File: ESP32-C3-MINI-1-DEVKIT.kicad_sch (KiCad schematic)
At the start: 8 parts, among them J1 USB_C_Receptacle_USB2.0, U1 ESP32-C3-MINI-1, U2 MCP1825S

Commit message: mostly done with cp2102
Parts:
- added C5: 10uF, symbol Device:C_Polarized_Small_US
- added C6: 0.1uF, symbol Device:C_Small
- added D1: SP0503BAHT, Package_TO_SOT_SMD:SOT-143, symbol Power_Protection:SP0503BAHT
- added D2: RED LED, symbol Device:LED
- added J2: CP2102_PROG, symbol Connector_Generic:Conn_01x04
- added Q1, Q2: MMSS8050, Package_TO_SOT_SMD:SOT-23, symbol Transistor_BJT:2N3055
- added R2: 22.1k, symbol Device:R_Small
- added R3: 47.5k, symbol Device:R_Small
- added R4: 1k, symbol Device:R
- added R5: 10k, symbol Device:R_Small
- added R6: 5k, symbol Device:R
- added R? (x2): 10k, symbol Device:R
- added U3: CP2102N-Axx-xQFN24, Package_DFN_QFN:QFN-24-1EP_4x4mm_P0.5mm_EP2.6x2.6mm, symbol Interface_USB:CP2102N-Axx-xQFN24
- gave numbers to parts that had none: 5
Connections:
- net 3V3_BUS: now also C5.1, C6.1, R4.1, U3.6 (VDD), U3.7 (VREGIN)
- net GNDREF: no longer C3.1, J1.A4 (VBUS), J1.A9 (VBUS), J1.B4 (VBUS), J1.B9 (VBUS), U2.1 (VI)
- net USB_D+: now also D1.4 (K), U3.3 (D+); no longer U1.27 (GPIO19/USB_D+)
- net USB_D-: now also D1.3 (K), U3.4 (D-); no longer U1.26 (GPIO18/USB_D-)
- net USB_GND: now also C5.2, C6.2, D1.1 (A), D2.1 (K), R3.2, R5.2, U3.2 (GND), U3.25 (GND)
- net GPIO9: now reaches U1.23 (GPIO9)
- net GPIO9: now also Q2.3 (C)
- net CP2102_TXD: now reaches U1.30 (GPIO20/U0RXD)
- net CP2102_TXD: now also U3.21 (TXD)
- net CP2102_RXD: now reaches U1.31 (GPIO21/U0TXD)
- net CP2102_RXD: now also U3.20 (RXD)
- new net: Q1.1 (B), R?.2
- new net: D2.2 (A), R6.1
- new net: J2.4 (Pin_4), U3.11 (~{WAKEUP}/GPIO.3)
- new net: J2.3 (Pin_3), U3.12 (RS485/GPIO.2)
- new net: J2.2 (Pin_2), U3.13 (~{RXT}/GPIO.1)
- new net: J2.1 (Pin_1), U3.14 (~{TXT}/GPIO.0)
- new net: R5.1, U3.15 (~{SUSPEND})
- new net: D1.2 (K), R2.2, R3.1, U3.8 (VBUS)
- new net: R4.2, U3.9 (~{RST})
- new net: Q2.1 (B), R?.2
- new net 5V_USB: C3.1, J1.A4 (VBUS), J1.A9 (VBUS), J1.B4 (VBUS), J1.B9 (VBUS), R2.1, R6.2, U2.1 (VI)
- new net CHIP_PU: Q1.3 (C)
- new net CP2102_DTR: Q2.2 (E), R?.1, U3.23 (~{DTR})
- new net CP2102_RTS: Q1.2 (E), R?.1, U3.19 (~{RTS})
- no-connect marks 4 -> 9
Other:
- note added: "Auto program DTR RTS-->EN IO9 1 1 1 1 0 0 1 1 1 0 0 1 0 1 1 0"
- note added: "TODO: TXT AND RXT PINS (14/13) GET LEDS TO SHOW STATUS"
- note added: "see https://dl.espressif.com/dl/schematics/SCH_ESP32-C3-DEVKITM-1_V1_20200915A.pdf for CHIP_PU"
- moved on the sheet: C1, C2, C3, C4, J1, R1, U1, U2

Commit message: Schematic v1 finished(?)
schematic finished and pcb layout ready to start for first time. schematic will very likely change
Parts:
- removed C1: 10uF, symbol Device:C
- removed C2: 0.1uF, symbol Device:C
- removed J2: CP2102_PROG, symbol Connector_Generic:Conn_01x04
- removed R1, R? (x2): 10k, symbol Device:R
- removed R4: 1k, symbol Device:R
- added C1: 1uF, symbol Device:C_Small
- added C2: 10uF, symbol Device:C_Small
- added C7: 0.1uF, symbol Device:C_Small
- added D3: SS1040_R1_00001, Diode_SMD:D_SOD-123, symbol Device:D_Small
- added D?: RX_LED_GREEN, symbol Device:LED
- added D?: TX_LED_BLUE, symbol Device:LED
- added J?: CP2102_OUTPUTS, symbol Connector_Generic:Conn_01x02
- added J?: C3_OUTPUTS, symbol Connector_Generic:Conn_01x12
- added R1, R4, R? (x2): 10k, Resistor_SMD:R_0805_2012Metric, symbol Device:R_Small
- added R9: 1k, Resistor_SMD:R_0805_2012Metric, symbol Device:R_Small
- added R? (x2): 2.2k, Resistor_SMD:R_0805_2012Metric, symbol Device:R_Small
- R2, R3, R5, R6: footprint (none) -> Resistor_SMD:R_0805_2012Metric
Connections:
- net GNDREF is gone; now on net USB_GND: U1.1 (GND), U1.11 (GND), U1.14 (GND), U1.2 (GND), U1.36 (GND)
- net 3V3_BUS: now also U3.5 (VIO), C2.1, C7.1, R1.1, R4.1, R9.1, R?.2, R?.2
- net 5V_USB: now also D3.1 (K); no longer J1.A4 (VBUS), J1.A9 (VBUS), J1.B4 (VBUS), J1.B9 (VBUS)
- net CHIP_PU: now also U1.8 (EN/CHIP_PU), C1.2, R1.2
- net CP2102_DTR: now also R?.1
- net CP2102_RTS: now also R?.1
- net GPIO9: now also J?.9 (Pin_9)
- net USB_GND: now also C1.1, C2.2, C7.2
- net at Q1.1 (B): now also R?.2
- net GPIO.3: now reaches U3.11 (~{WAKEUP}/GPIO.3)
- net GPIO.3: now also J?.2 (Pin_2)
- net GPIO.2: now reaches U3.12 (RS485/GPIO.2)
- net GPIO.2: now also J?.1 (Pin_1)
- net GPIO.1: now reaches U3.13 (~{RXT}/GPIO.1)
- net GPIO.1: now also D?.1 (K)
- net GPIO.0: now reaches U3.14 (~{TXT}/GPIO.0)
- net GPIO.0: now also D?.1 (K)
- net at U3.9 (~{RST}): now also R9.2
- net at U1.22 (GPIO8): now also R4.2
- net at Q2.1 (B): now also R?.2
- net GPIO0: now reaches U1.12 (GPIO0/ADC1_CH0/XTAL_32K_P)
- net GPIO0: now also J?.1 (Pin_1)
- net GPIO1: now reaches U1.13 (GPIO1/ADC1_CH1/XTAL_32K_N)
- net GPIO1: now also J?.2 (Pin_2)
- net GPIO10: now reaches U1.16 (GPIO10)
- net GPIO10: now also J?.10 (Pin_10)
- net GPIO4: now reaches U1.18 (GPIO4/ADC1_CH4)
- net GPIO4: now also J?.5 (Pin_5)
- net GPIO5: now reaches U1.19 (GPIO5/ADC2_CH0)
- net GPIO5: now also J?.6 (Pin_6)
- net GPIO6: now reaches U1.20 (GPIO6)
- net GPIO6: now also J?.7 (Pin_7)
- net GPIO7: now reaches U1.21 (GPIO7)
- net GPIO7: now also J?.8 (Pin_8)
- net GPIO18: now reaches U1.26 (GPIO18/USB_D-)
- net GPIO18: now also J?.11 (Pin_11)
- net GPIO19: now reaches U1.27 (GPIO19/USB_D+)
- net GPIO19: now also J?.12 (Pin_12)
- net GPIO2: now reaches U1.5 (GPIO2/ADC1_CH2)
- net GPIO2: now also J?.3 (Pin_3)
- net GPIO3: now reaches U1.6 (GPIO3/ADC1_CH3)
- net GPIO3: now also J?.4 (Pin_4)
- new net: D?.2 (A), R?.1 (x2)
- new net: D3.2 (A), J1.A4 (VBUS), J1.A9 (VBUS), J1.B4 (VBUS), J1.B9 (VBUS)
- no-connect marks 9 -> 10
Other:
- note added: "FROM C3 MINI"
- note added: "FROM CP2102"
- note added: "OUTPUTS"
- note added: "POWER - 5V TO 3.3V"
- note added: "RS485"
- note added: "~WAKEUP"
- note removed: "5V TO 3.3V"
- moved on the sheet: J1

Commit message: lots of updates, started layout
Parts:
- removed C4: 1uF, symbol Device:C
- removed C5: 10uF, symbol Device:C_Polarized_Small_US
- added C4: 1uF, Capacitor_SMD:C_0805_2012Metric, symbol Device:C_Small
- added C5: 0.1uF, Capacitor_SMD:C_0805_2012Metric, symbol Device:C_Small
- added SW1, SW2: TL6330AF200Q, Button_Switch_SMD:SW_Push_1P1T_NO_CK_KMR2, symbol Switch:SW_MEC_5E
- C1, C6, C7: footprint (none) -> Capacitor_SMD:C_0805_2012Metric
- C2, C3: footprint (none) -> Capacitor_SMD:CP_Elec_5x5.3
- D2: footprint (none) -> LED_SMD:LED_0603_1608Metric
- D4, D5: renamed from D?; footprint (none) -> LED_SMD:LED_0603_1608Metric
- U1: footprint Espressif:ESP32-C3-MINI-1 -> ESP:ESP32-C3-MINI-1
- gave numbers to parts that had none: 6
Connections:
- net 3V3_BUS: now also C4.1, C5.1; no longer C6.1, C7.1
- net CHIP_PU: now also C7.2, SW2.4 (A)
- net GPIO9: now also C6.2, SW1.4 (A)
- net USB_GND: now also C6.1, C7.1, C4.2, C5.2, SW1.1, SW2.1; no longer C6.2, C7.2
- no-connect marks 10 -> 13
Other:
- note added: "CP2102"
- note added: "ESP32-C3-MINI-1"
- note added: "Layout notes: 1. *done* 2. TODO: button footprints 3. USB-C 3D model needed 4. ESP32-C3-MINI-1 3D model needed 5. can upgrade electrolytics to tantalum for better footprint"
- note added: "PHYSICAL BUTTONS"
- note added: "RTS AND DTR LOGIC"
- note added: "these switch devices are probably wrong (triple check symbol + footprint)"
- note removed: "TODO: TXT AND RXT PINS (14/13) GET LEDS TO SHOW STATUS"
- moved on the sheet: C1, C3, D1, D2, D3, D4, D5, J1, J2, J3, Q1, Q2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

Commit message: layout progress
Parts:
- removed J2: C3_OUTPUTS, symbol Connector_Generic:Conn_01x12
- added J2: MINI_OUTS_1, Connector_PinHeader_2.54mm:PinHeader_1x06_P2.54mm_Vertical, symbol Connector_Generic:Conn_01x06
- added J4: MINI_OUTS_2, Connector_PinHeader_2.54mm:PinHeader_1x06_P2.54mm_Vertical, symbol Connector_Generic:Conn_01x06
- added J5: PWR_OUTPUTS, Connector_PinHeader_2.54mm:PinHeader_1x04_P2.54mm_Vertical, symbol Connector_Generic:Conn_01x04
- J3: footprint (none) -> Connector_PinHeader_2.54mm:PinHeader_1x02_P2.54mm_Vertical
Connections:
- net 3V3_BUS: now also J5.4 (Pin_4)
- net GPIO0: now also J2.1 (Pin_1)
- net GPIO1: now also J2.2 (Pin_2)
- net GPIO10: now also J4.4 (Pin_4)
- net GPIO18: now also J4.5 (Pin_5)
- net GPIO19: now also J4.6 (Pin_6)
- net GPIO2: now also J2.3 (Pin_3)
- net GPIO3: now also J2.4 (Pin_4)
- net GPIO4: now also J2.5 (Pin_5)
- net GPIO5: now also J2.6 (Pin_6)
- net GPIO6: now also J4.1 (Pin_1)
- net GPIO7: now also J4.2 (Pin_2)
- net GPIO9: now also J4.3 (Pin_3)
- net USB_GND: now also J5.2 (Pin_2), J5.3 (Pin_3)
- net VBUS_5V: now reaches D3.2 (A), J1.A4 (VBUS), J1.A9 (VBUS), J1.B4 (VBUS), J1.B9 (VBUS)
- net VBUS_5V: now also J5.1 (Pin_1)

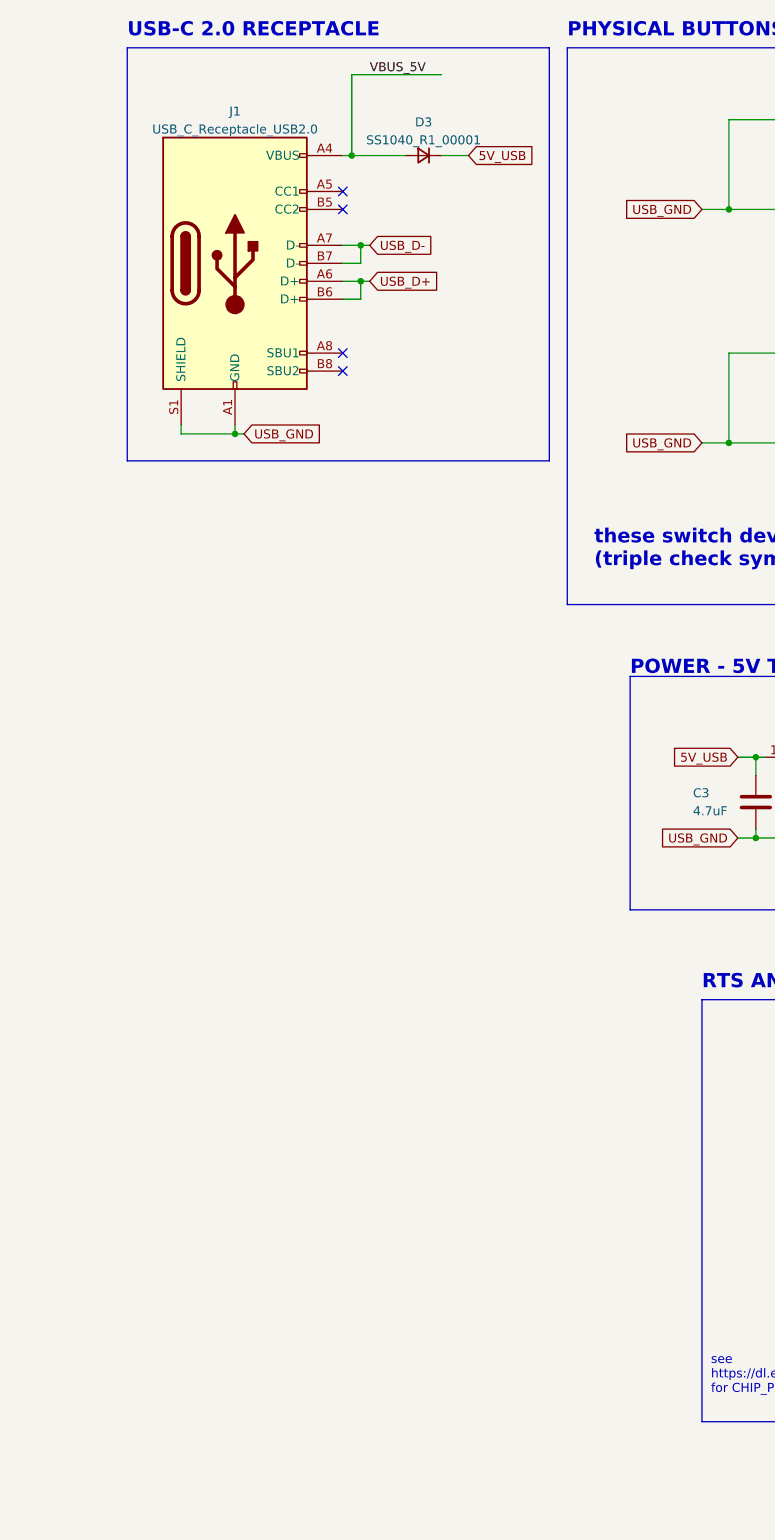
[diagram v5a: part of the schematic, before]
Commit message: silkscreen done
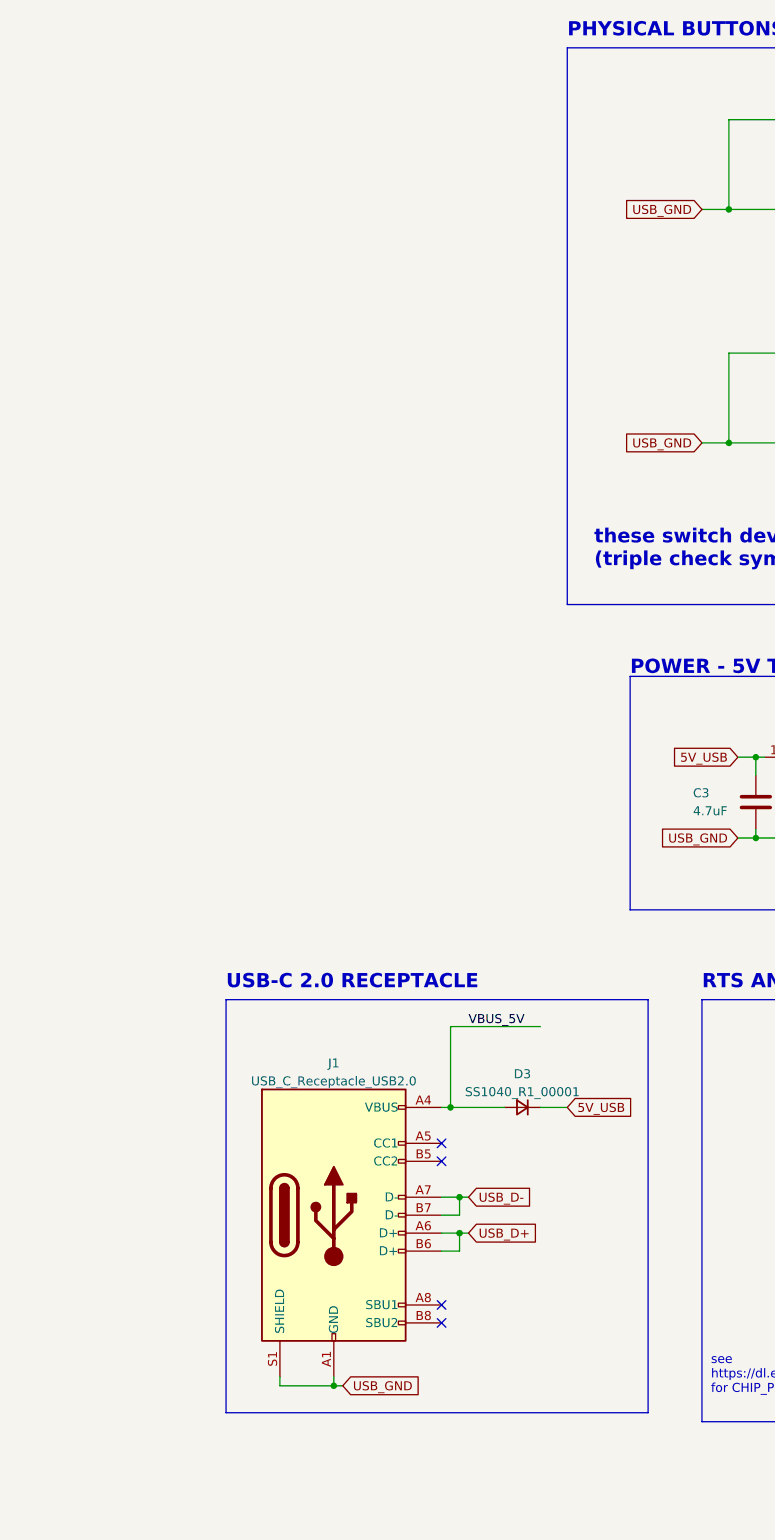
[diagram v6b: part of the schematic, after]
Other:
- moved on the sheet: D3, J1
